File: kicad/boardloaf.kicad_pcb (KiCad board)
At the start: 2 copper layers, 100 x 100 mm, 43 parts, among them J1 AudioJack4, J2 AudioJack4, SW1 SW_Push, SW10 SW_Push, SW11 SW_Push, SW12 SW_Push, SW13 SW_Push, SW14 SW_Push, SW15 SW_Push, SW16 SW_Push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

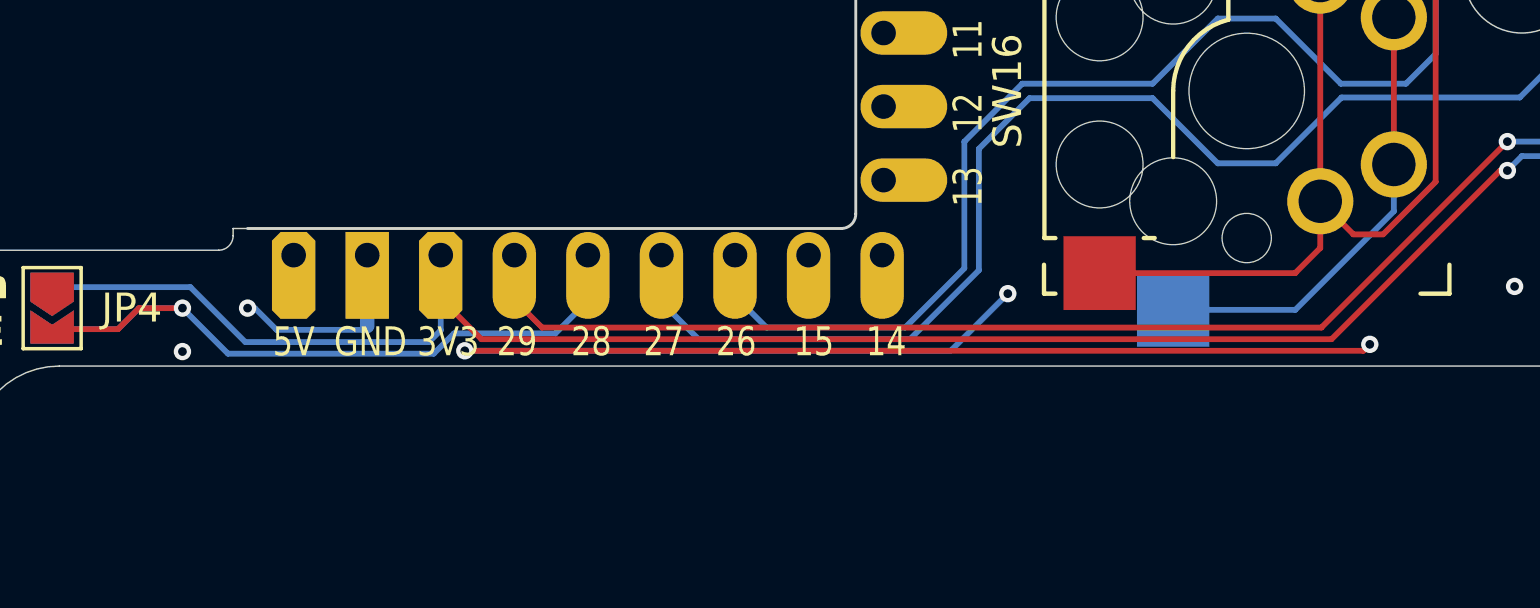
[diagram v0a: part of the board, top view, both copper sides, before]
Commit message: update ground route and gubber
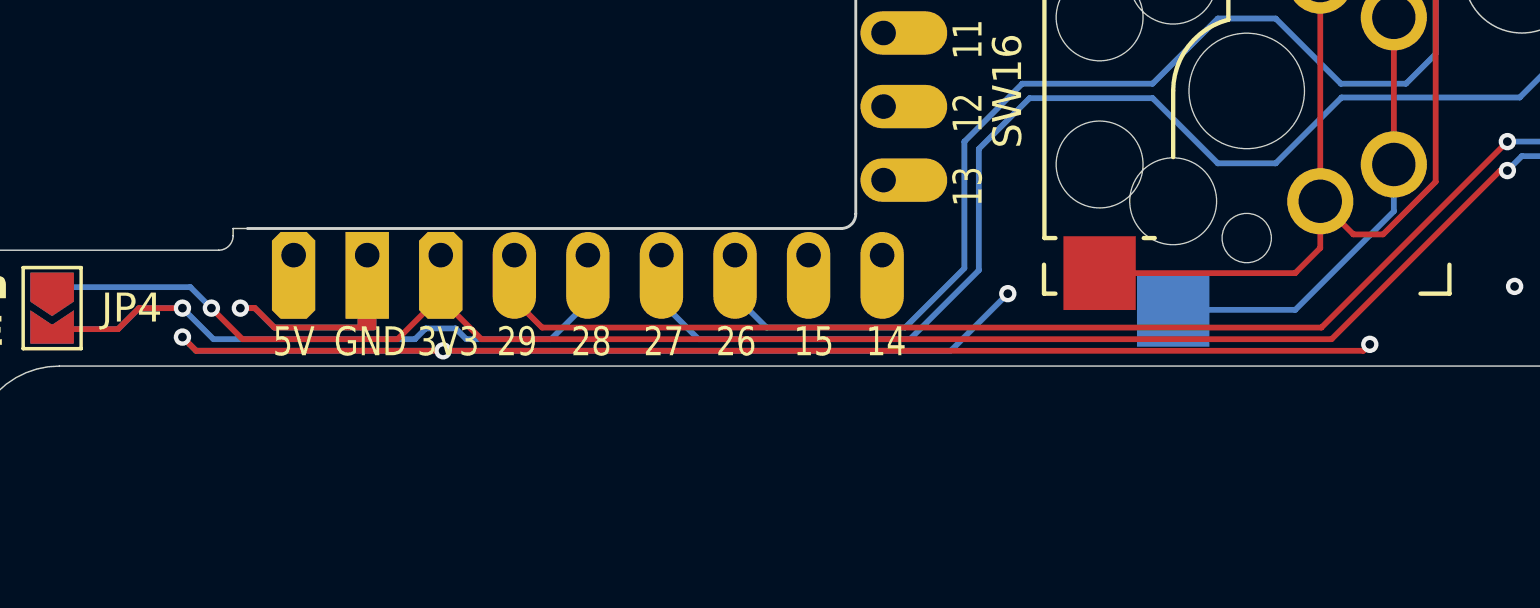
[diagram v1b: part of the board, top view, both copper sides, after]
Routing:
- net GND: track 57.9 -> 79.3 mm
- net VCC: track 97.6 -> 95.7 mm, vias 1 -> 2
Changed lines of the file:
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@@
 		)
 	)
+	(gr_rect
+		(start 91.9 133.22)
+		(end 92.35 135.17)
+		(stroke
+			(width 0.2)
+			(type default)
+		)
+		(fill yes)
+		(layer "F.Cu")
+		(net 23)
+	)
+	(gr_line
+		(start 85.75 135.5)
+		(end 86 135.75)
+		(stroke
+			(width 0.2)
+			(type default)
+		)
+		(layer "F.Cu")
+		(net 23)
+	)
+	(gr_line
+		(start 87.75 134.5)
+		(end 88.15 134.5)
+		(stroke
+			(width 0.2)
+			(type default)
+		)
+		(layer "F.Cu")
+		(net 23)
+	)
+	(gr_rect
+		(start 91.9 133.22)
+		(end 92.35 135.17)
+		(stroke
+			(width 0.2)
+			(type default)
+		)
+		(fill yes)
+		(layer "B.Cu")
+		(net 23)
+	)
 	(gr_arc
 		(start 78.500003 139.499998)
@@
 	)
 	(segment
-		(start 95.5 135.973)
+		(start 88.921 135.171)
+		(end 92.15 135.171)
+		(width 0.2)
+		(layer "F.Cu")
+		(net 23)
+	)
+	(segment
+		(start 94.75 135.973)
+		(end 86.223 135.973)
+		(width 0.2)
+		(layer "F.Cu")
+		(net 23)
+	)
+	(segment
+		(start 88.25 134.5)
+		(end 88.921 135.171)
+		(width 0.2)
+		(layer "F.Cu")
+		(net 23)
+	)
+	(segment
+		(start 88.15 134.5)
+		(end 88.25 134.5)
+		(width 0.2)
+		(layer "F.Cu")
+		(net 23)
+	)
+	(segment
+		(start 86.223 135.973)
+		(end 86 135.75)
+		(width 0.2)
+		(layer "F.Cu")
+		(net 23)
+	)
+	(segment
+		(start 94.75 135.973)
 		(end 126.527 135.973)
 		(width 0.2)
@@
 	)
 	(via
-		(at 95.5 135.973)
+		(at 94.75 135.973)
 		(size 0.6)
 		(drill 0.3)
@@
 	)
 	(via
-		(at 85.75 136)
+		(at 85.75 135.5)
 		(size 0.6)
 		(drill 0.3)
@@
 	)
 	(via
-		(at 88 134.5)
+		(at 87.75 134.5)
 		(size 0.6)
 		(drill 0.3)
@@
 	)
 	(segment
-		(start 89 135.25)
-		(end 92 135.25)
+		(start 94.75 135.973)
+		(end 86.223 135.973)
 		(width 0.2)
 		(layer "B.Cu")
@@
 	)
 	(segment
-		(start 92.13 135.12)
-		(end 92.13 132.67)
-		(width 0.5)
+		(start 112.277 135.973)
+		(end 114.25 134)
+		(width 0.2)
 		(layer "B.Cu")
 		(net 23)
@@
 	(segment
 		(start 88.25 134.5)
-		(end 89 135.25)
+		(end 88.921 135.171)
 		(width 0.2)
 		(layer "B.Cu")
@@
 	)
 	(segment
-		(start 92 135.25)
-		(end 92.13 135.12)
+		(start 86.223 135.973)
+		(end 85.75 135.5)
 		(width 0.2)
 		(layer "B.Cu")
@@
 	)
 	(segment
-		(start 88 134.5)
-		(end 88.25 134.5)
+		(start 94.75 135.973)
+		(end 112.277 135.973)
 		(width 0.2)
 		(layer "B.Cu")
@@
 	)
 	(segment
-		(start 95.5 135.973)
-		(end 112.277 135.973)
+		(start 88.921 135.171)
+		(end 92.079 135.171)
 		(width 0.2)
 		(layer "B.Cu")
@@
 	)
 	(segment
-		(start 112.277 135.973)
-		(end 114.25 134)
+		(start 87.75 134.5)
+		(end 88.25 134.5)
 		(width 0.2)
 		(layer "B.Cu")
@@
 	)
 	(segment
+		(start 94.67 134.08)
+		(end 94.67 132.67)
+		(width 0.2)
+		(layer "F.Cu")
+		(net 31)
+	)
+	(segment
+		(start 87.822 135.572)
+		(end 93.178 135.572)
+		(width 0.2)
+		(layer "F.Cu")
+		(net 31)
+	)
+	(segment
 		(start 125.428 135.572)
 		(end 131.25 129.75)
@@
 	)
 	(segment
-		(start 94.67 132.67)
-		(end 94.67 133.83)
+		(start 93.178 135.572)
+		(end 94.67 134.08)
 		(width 0.2)
 		(layer "F.Cu")
@@
 	)
 	(segment
+		(start 86.75 134.5)
+		(end 87.822 135.572)
+		(width 0.2)
+		(layer "F.Cu")
+		(net 31)
+	)
+	(segment
 		(start 156.8 113.7)
 		(end 156.8 118.3)
@@
 		(net 31)
 	)
+	(via
+		(at 86.75 134.5)
+		(size 0.6)
+		(drill 0.3)
+		(layers "F.Cu" "B.Cu")
+		(net 31)
+	)
 	(segment
-		(start 87.921 135.671)
-		(end 86.025 133.775)
+		(start 86.025 133.775)
+		(end 86.75 134.5)
 		(width 0.2)
 		(layer "B.Cu")
@@
 	)
 	(segment
-		(start 94.67 135.2629)
-		(end 94.2619 135.671)
-		(width 0.2)
-		(layer "B.Cu")
-		(net 31)
-	)
-	(segment
-		(start 94.2619 135.671)
-		(end 87.921 135.671)
-		(width 0.2)
-		(layer "B.Cu")
-		(net 31)
-	)
-	(segment
 		(start 144.75 129.25)
 		(end 148.753 129.25)
@@
 	)
 	(segment
-		(start 94.67 132.67)
-		(end 94.67 135.2629)
-		(width 0.2)
-		(layer "B.Cu")
-		(net 31)
-	)
-	(segment
 		(start 138.258855 129.25)
 		(end 140.500001 131.491146)
@@
 	)
 	(segment
-		(start 98.628 135.372)
-		(end 95.128 135.372)
+		(start 95.55 135.572)
+		(end 98.478 135.572)
 		(width 0.2)
 		(layer "B.Cu")
@@
 	)
 	(segment
-		(start 95.128 135.372)
-		(end 94.428 136.072)
+		(start 85.75 134.5)
+		(end 84.25 134.5)
 		(width 0.2)
 		(layer "B.Cu")
@@
 	)
 	(segment
-		(start 85.75 134.5)
-		(end 84.25 134.5)
+		(start 95.178 135.2)
+		(end 95.55 135.572)
 		(width 0.2)
 		(layer "B.Cu")
@@
 	)
 	(segment
-		(start 99.75 134.25)
-		(end 98.628 135.372)
+		(start 94.15 135.2)
+		(end 95.178 135.2)
 		(width 0.2)
 		(layer "B.Cu")
@@
 	)
 	(segment
-		(start 99.75 132.67)
-		(end 99.75 134.25)
+		(start 98.478 135.572)
+		(end 99.75 134.3)
 		(width 0.2)
 		(layer "B.Cu")
@@
 	)
 	(segment
-		(start 83.525 135.225)
-		(end 81.25 135.225)
+		(start 99.75 134.3)
+		(end 99.75 132.67)
+		(width 0.2)
+		(layer "B.Cu")
+		(net 36)
+	)
+	(segment
+		(start 85.75 134.5)
+		(end 86.822 135.572)
 		(width 0.2)
 		(layer "B.Cu")
@@
 	)
 	(segment
-		(start 94.428 136.072)
-		(end 87.322 136.072)
+		(start 86.822 135.572)
+		(end 93.778 135.572)
+		(width 0.2)
+		(layer "B.Cu")
+		(net 36)
+	)
+	(segment
+		(start 83.525 135.225)
+		(end 81.25 135.225)
 		(width 0.2)
 		(layer "B.Cu")
@@
 	)
 	(segment
-		(start 87.322 136.072)
-		(end 85.75 134.5)
+		(start 93.778 135.572)
+		(end 94.15 135.2)
 		(width 0.2)
 		(layer "B.Cu")
